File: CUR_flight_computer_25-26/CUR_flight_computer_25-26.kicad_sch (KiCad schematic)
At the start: 0 parts

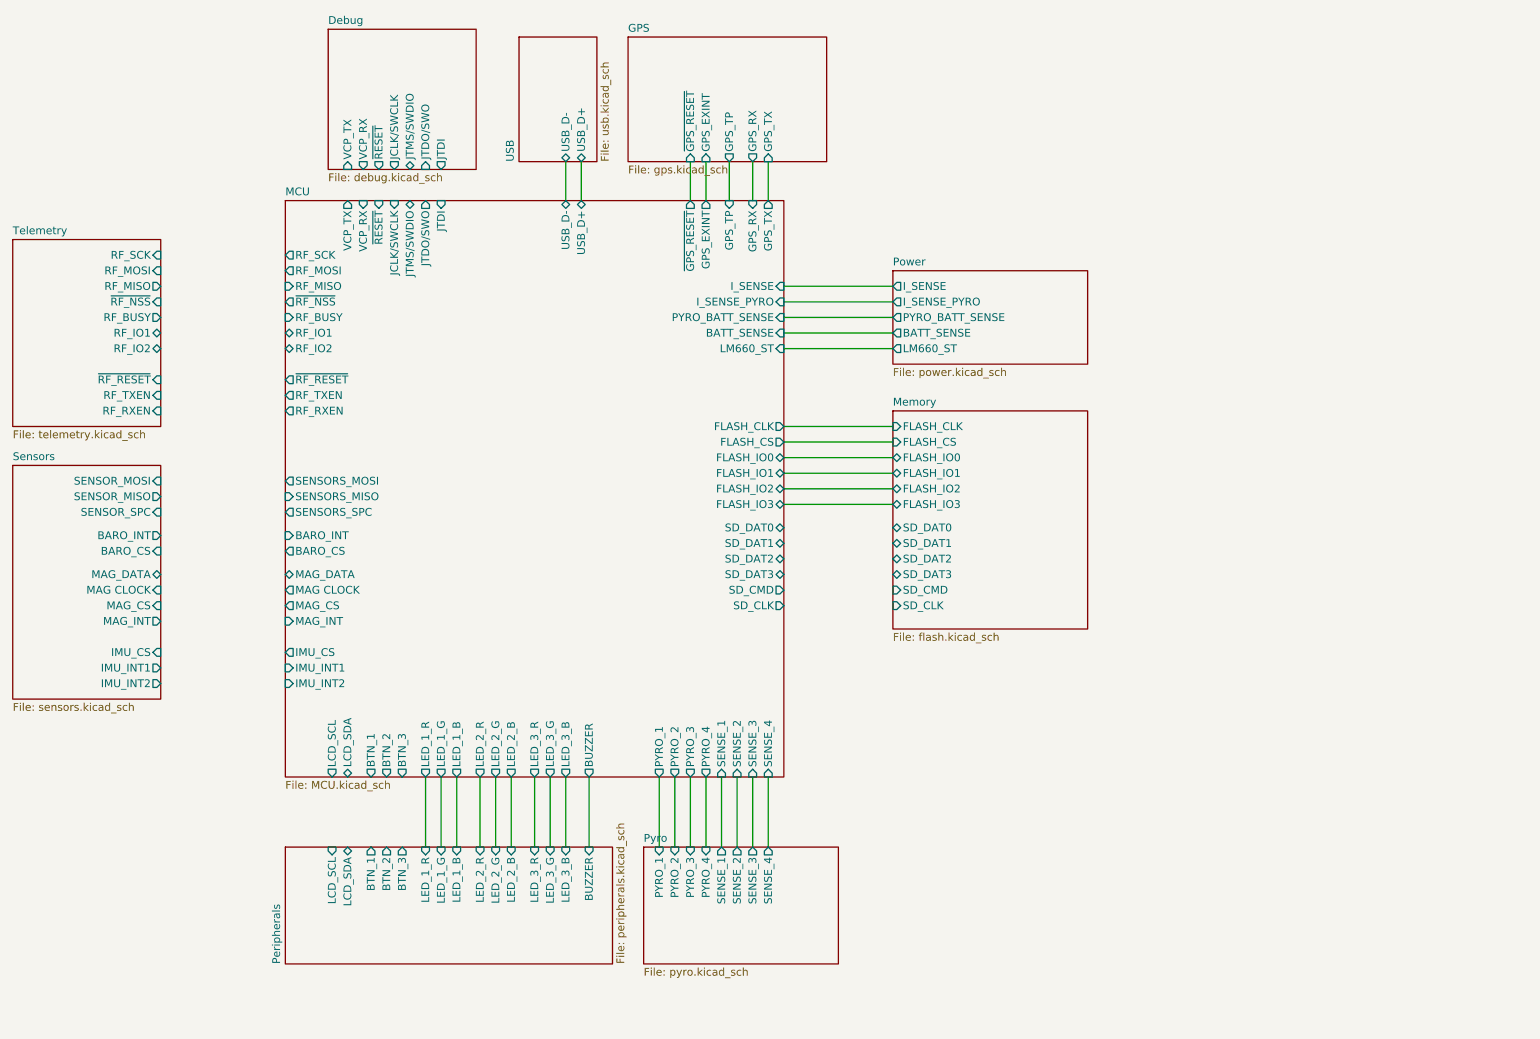
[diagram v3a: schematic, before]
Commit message: updated pinout
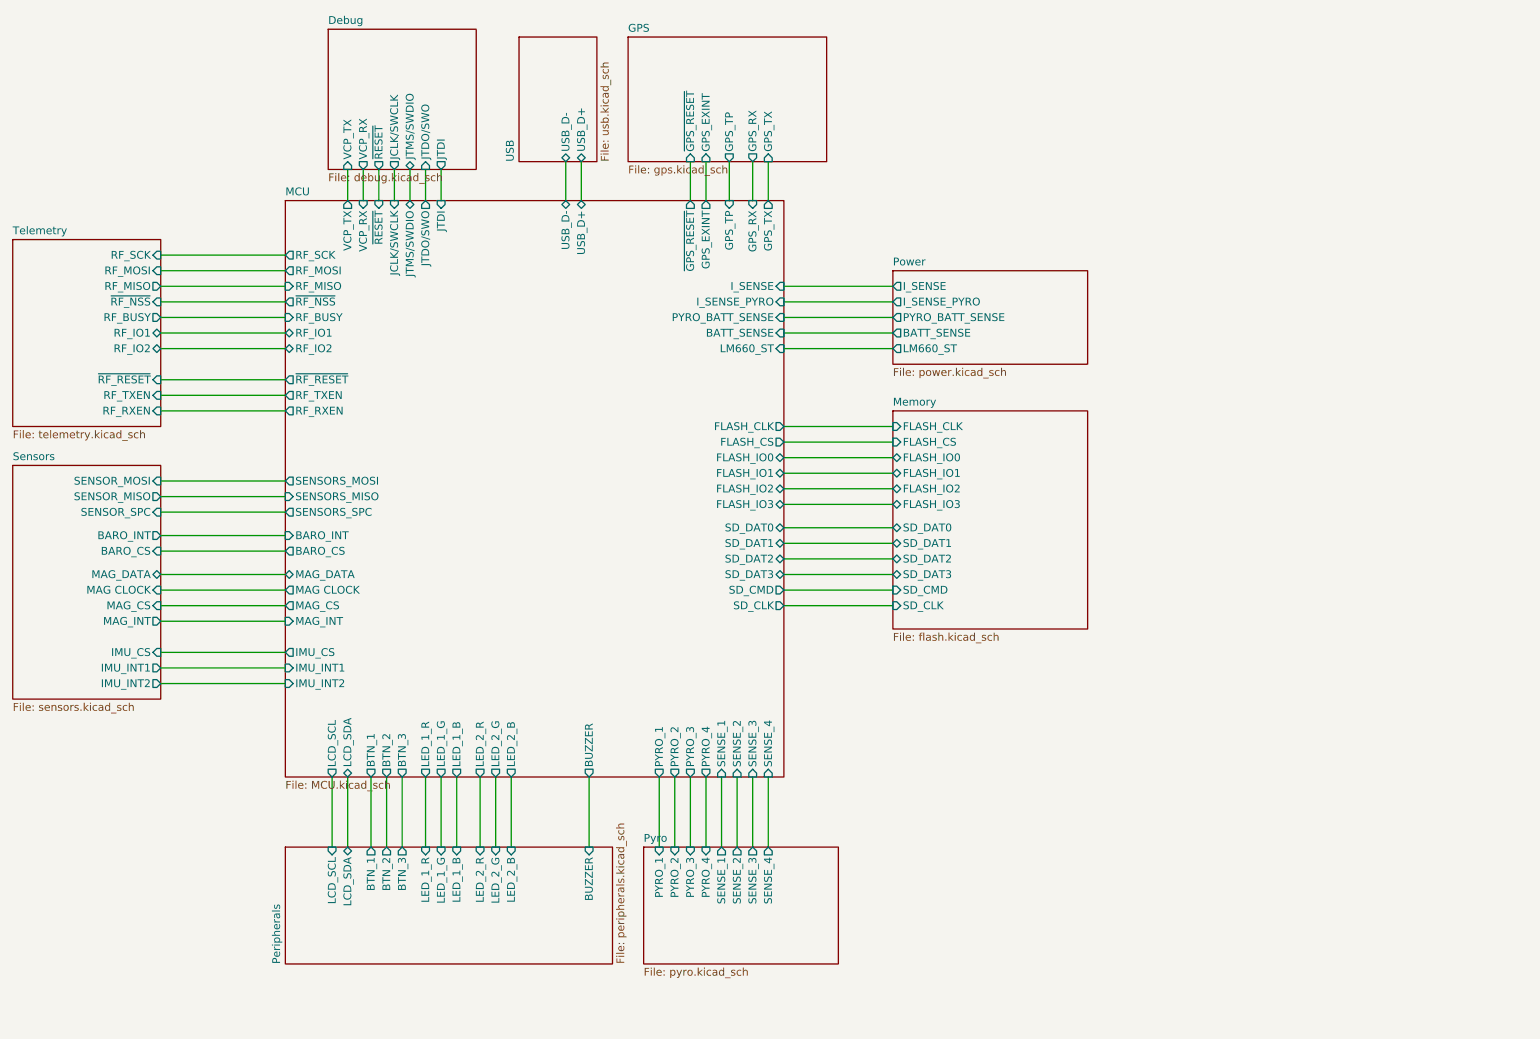
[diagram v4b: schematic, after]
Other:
- sheet MCU ports: added none; removed LED_3_B, LED_3_G, LED_3_R
- sheet Peripherals ports: added none; removed LED_3_B, LED_3_G, LED_3_R

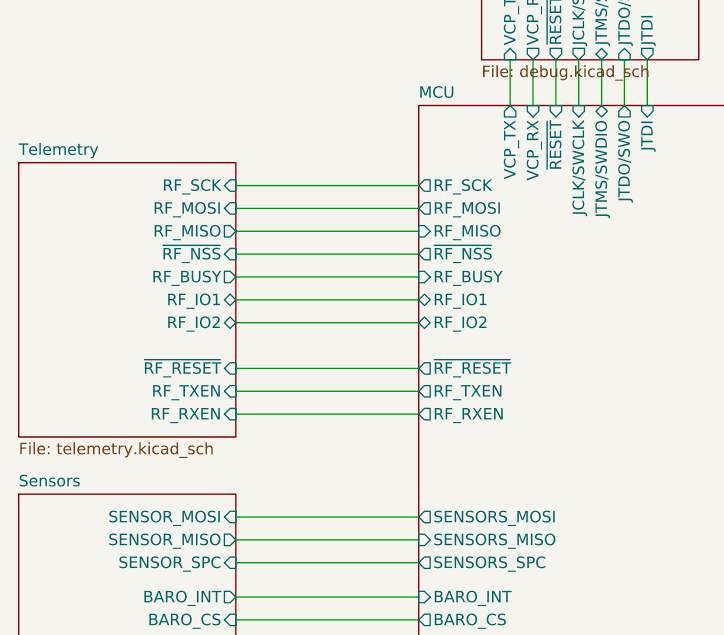
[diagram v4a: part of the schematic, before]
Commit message: updated rf module to ebyte-lora-400MM-22s
added footprint
added symbol
updates schematic
updated pcb
need to reroute
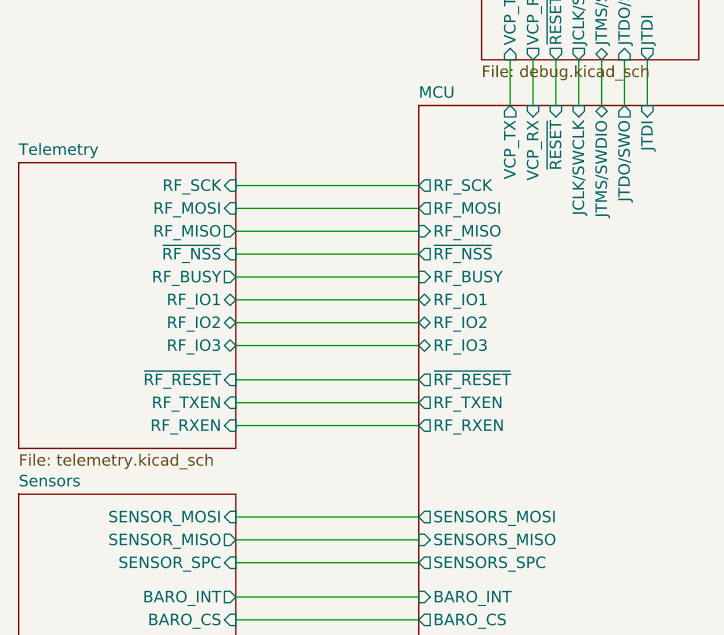
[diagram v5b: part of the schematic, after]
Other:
- sheet MCU ports: added RF_IO3; removed none
- sheet Telemetry ports: added RF_IO3; removed none
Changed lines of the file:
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@@
 	(wire
 		(pts
-			(xy 60.96 74.93) (xy 81.28 74.93)
+			(xy 60.96 76.2) (xy 81.28 76.2)
 		)
 		(stroke
@@
 	(wire
 		(pts
-			(xy 60.96 80.01) (xy 81.28 80.01)
+			(xy 60.96 81.28) (xy 81.28 81.28)
+		)
+		(stroke
+			(width 0)
+			(type default)
+		)
+	)
+	(wire
+		(pts
+			(xy 60.96 72.39) (xy 81.28 72.39)
 		)
 		(stroke
@@
 	(wire
 		(pts
-			(xy 60.96 77.47) (xy 81.28 77.47)
+			(xy 60.96 78.74) (xy 81.28 78.74)
 		)
 		(stroke
@@
 	(sheet
 		(at 36.83 52.07)
-		(size 24.13 30.48)
+		(size 24.13 31.75)
 		(exclude_from_sim no)
 		(in_bom yes)
@@
 		)
 		(property "Sheetfile" "telemetry.kicad_sch"
-			(at 36.83 83.1346 0)
+			(at 36.83 84.4046 0)
 			(effects
 				(font
@@
 		)
 		(pin "~{RF_RESET}" input
-			(at 60.96 74.93 0)
+			(at 60.96 76.2 0)
 			(effects
 				(font
@@
 		)
 		(pin "RF_TXEN" input
-			(at 60.96 77.47 0)
+			(at 60.96 78.74 0)
 			(effects
 				(font
@@
 		)
 		(pin "RF_RXEN" input
-			(at 60.96 80.01 0)
+			(at 60.96 81.28 0)
+			(effects
+				(font
+					(size 1.27 1.27)
+				)
+				(justify right)
+			)
+		)
+		(pin "RF_IO3" bidirectional
+			(at 60.96 72.39 0)
 			(effects
 				(font
@@
 		)
 		(pin "~{RF_RESET}" output
-			(at 81.28 74.93 180)
+			(at 81.28 76.2 180)
 			(effects
 				(font
@@
 		)
 		(pin "RF_RXEN" output
-			(at 81.28 80.01 180)
+			(at 81.28 81.28 180)
 			(effects
 				(font
@@
 		)
 		(pin "RF_TXEN" output
-			(at 81.28 77.47 180)
+			(at 81.28 78.74 180)
 			(effects
 				(font
@@
 			(effects
 				(font
+					(size 1.27 1.27)
+				)
+				(justify left)
+			)
+		)
+		(pin "RF_IO3" bidirectional
+			(at 81.28 72.39 180)
+			(effects
+				(font

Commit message: Remove JTDI and combine NRST and ~{RESET}
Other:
- sheet Debug ports: added none; removed JTDI
- sheet MCU ports: added none; removed JTDI
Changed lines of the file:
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@@
-	(wire
-		(pts
-			(xy 106.68 40.64) (xy 106.68 45.72)
-		)
-		(stroke
-			(width 0)
-			(type default)
-		)
-	)
 	(wire
 		(pts
@@
 			)
 		)
-		(pin "JTDI" output
-			(at 106.68 40.64 270)
-			(effects
-				(font
-					(size 1.27 1.27)
-				)
-				(justify left)
-			)
-		)
 		(pin "~{RESET}" output
 			(at 96.52 40.64 270)
@@
 			(effects
 				(font
-					(size 1.27 1.27)
-				)
-				(justify right)
-			)
-		)
-		(pin "JTDI" input
-			(at 106.68 45.72 90)
-			(effects
-				(font

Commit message: Cleaned up schematic
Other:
- company: (none) -> Clarkson University Rocketry
- title: (none) -> Flight Computer
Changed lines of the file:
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@@
 	(generator_version "9.0")
 	(paper "A4")
+	(title_block
+		(title "Flight Computer")
+		(date "2026-03-18")
+		(company "Clarkson University Rocketry")
+	)
 	(wire
 		(pts
@@
 			(width 0)
 			(type default)
+		)
+	)
+	(symbol
+		(lib_id "CUR_Logo:LOGO")
+		(at 279.4 173.99 0)
+		(unit 1)
+		(exclude_from_sim no)
+		(in_bom yes)
+		(on_board yes)
+		(dnp no)
+		(fields_autoplaced yes)
+		(property "Reference" "#G1"
+			(at 279.4 167.002 0)
+			(effects
+				(font
+					(size 1.27 1.27)
+				)
+				(hide yes)
+			)
+		)
+		(property "Value" "LOGO"
+			(at 279.4 180.978 0)
+			(effects
+				(font
+					(size 1.27 1.27)
+				)
+				(hide yes)
+			)
+		)
+		(property "Footprint" ""
+			(at 279.4 173.99 0)
+			(effects
+				(font
+					(size 1.27 1.27)
+				)
+				(hide yes)
+			)
+		)
+		(property "Datasheet" ""
+			(at 279.4 173.99 0)
+			(effects
+				(font
+					(size 1.27 1.27)
+				)
+				(hide yes)
+			)
+		)
+		(property "Description" ""
+			(at 279.4 173.99 0)
+			(effects
+				(font
+					(size 1.27 1.27)
+				)
+				(hide yes)
+			)
+		)
+		(instances
+			(project "CUR_flight_computer_25-26"
+				(path "/bf7761cc-1b32-4d86-809c-5f027005229b"
+					(reference "#G1")
+					(unit 1)
+				)
+			)
 		)
 	)
@@
 			)
 		)
-		(pin "BTN_1" output
+		(pin "BTN_1" input
 			(at 95.25 139.7 270)
 			(effects
@@
 			)
 		)
-		(pin "BTN_2" output
+		(pin "BTN_2" input
 			(at 97.79 139.7 270)
 			(effects
@@
 			)
 		)
-		(pin "BTN_3" output
+		(pin "BTN_3" input
 			(at 100.33 139.7 270)
 			(effects

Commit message: Connect GPS I2C to LCD I2C
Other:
- sheet GPS ports: added GPS_SCL, GPS_SDA; removed none
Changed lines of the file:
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@@
 		(company "Clarkson University Rocketry")
 	)
+	(junction
+		(at 88.9 144.78)
+		(diameter 0)
+		(color 0 0 0 0)
+	)
+	(junction
+		(at 91.44 147.32)
+		(diameter 0)
+		(color 0 0 0 0)
+	)
 	(wire
 		(pts
@@
 	(wire
 		(pts
-			(xy 91.44 139.7) (xy 91.44 151.13)
+			(xy 91.44 139.7) (xy 91.44 147.32)
 		)
 		(stroke
@@
 	(wire
 		(pts
-			(xy 88.9 139.7) (xy 88.9 151.13)
+			(xy 88.9 139.7) (xy 88.9 144.78)
 		)
 		(stroke
@@
 	(wire
 		(pts
+			(xy 72.39 147.32) (xy 91.44 147.32)
+		)
+		(stroke
+			(width 0)
+			(type default)
+		)
+	)
+	(wire
+		(pts
 			(xy 162.56 85.09) (xy 180.34 85.09)
 		)
@@
 	(wire
 		(pts
+			(xy 181.61 24.13) (xy 171.45 24.13)
+		)
+		(stroke
+			(width 0)
+			(type default)
+		)
+	)
+	(wire
+		(pts
 			(xy 60.96 111.76) (xy 81.28 111.76)
 		)
@@
 	(wire
 		(pts
+			(xy 88.9 144.78) (xy 88.9 151.13)
+		)
+		(stroke
+			(width 0)
+			(type default)
+		)
+	)
+	(wire
+		(pts
 			(xy 149.86 139.7) (xy 149.86 151.13)
 		)
@@
 	(wire
 		(pts
+			(xy 72.39 144.78) (xy 88.9 144.78)
+		)
+		(stroke
+			(width 0)
+			(type default)
+		)
+	)
+	(wire
+		(pts
 			(xy 60.96 76.2) (xy 81.28 76.2)
 		)
@@
 	(wire
 		(pts
+			(xy 91.44 147.32) (xy 91.44 151.13)
+		)
+		(stroke
+			(width 0)
+			(type default)
+		)
+	)
+	(wire
+		(pts
 			(xy 153.67 39.37) (xy 153.67 45.72)
 		)
@@
 	(wire
 		(pts
+			(xy 171.45 26.67) (xy 181.61 26.67)
+		)
+		(stroke
+			(width 0)
+			(type default)
+		)
+	)
+	(wire
+		(pts
 			(xy 180.34 59.69) (xy 162.56 59.69)
 		)
@@
 			(width 0)
 			(type default)
+		)
+	)
+	(label "LCD_SCL"
+		(at 181.61 26.67 180)
+		(effects
+			(font
+				(size 1.27 1.27)
+			)
+			(justify right bottom)
+		)
+	)
+	(label "LCD_SCL"
+		(at 72.39 144.78 0)
+		(effects
+			(font
+				(size 1.27 1.27)
+			)
+			(justify left bottom)
+		)
+	)
+	(label "LCD_SDA"
+		(at 181.61 24.13 180)
+		(effects
+			(font
+				(size 1.27 1.27)
+			)
+			(justify right bottom)
+		)
+	)
+	(label "LCD_SDA"
+		(at 72.39 147.32 0)
+		(effects
+			(font
+				(size 1.27 1.27)
+			)
+			(justify left bottom)
 		)
 	)
@@
 	(sheet
 		(at 137.16 19.05)
-		(size 32.385 20.32)
+		(size 34.29 20.32)
 		(exclude_from_sim no)
 		(in_bom yes)
@@
 			)
 		)
+		(pin "GPS_SCL" input
+			(at 171.45 26.67 0)
+			(effects
+				(font
+					(size 1.27 1.27)
+				)
+				(justify right)
+			)
+		)
+		(pin "GPS_SDA" bidirectional
+			(at 171.45 24.13 0)
+			(effects
+				(font
+					(size 1.27 1.27)
+				)
+				(justify right)
+			)
+		)
